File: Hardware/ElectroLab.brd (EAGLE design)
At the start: 175 x 100 mm, 244 parts, among them IC1 LM2902DT, IC10 CD4511BNSR, IC11 PAM8403, IC12 LM2902DT, IC13 ADXL337, IC14 MIC5205, IC2 LM2902DT, IC3 SN74LV08ADR, IC4 SN74LV32ADR, IC5 SN74LV04ADR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

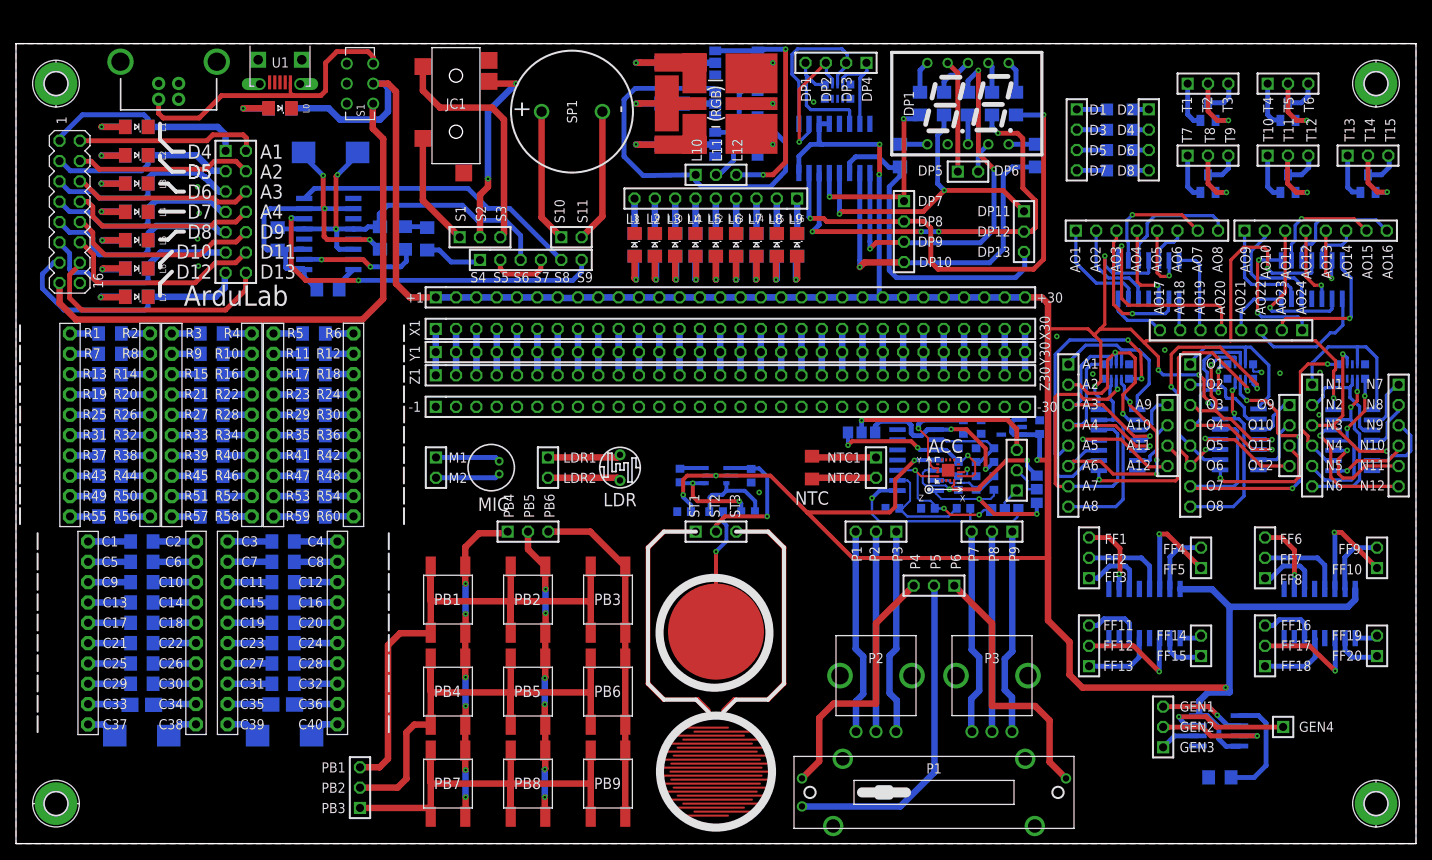
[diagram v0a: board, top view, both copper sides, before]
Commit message: Removed Amplifier after Acc ADXL337
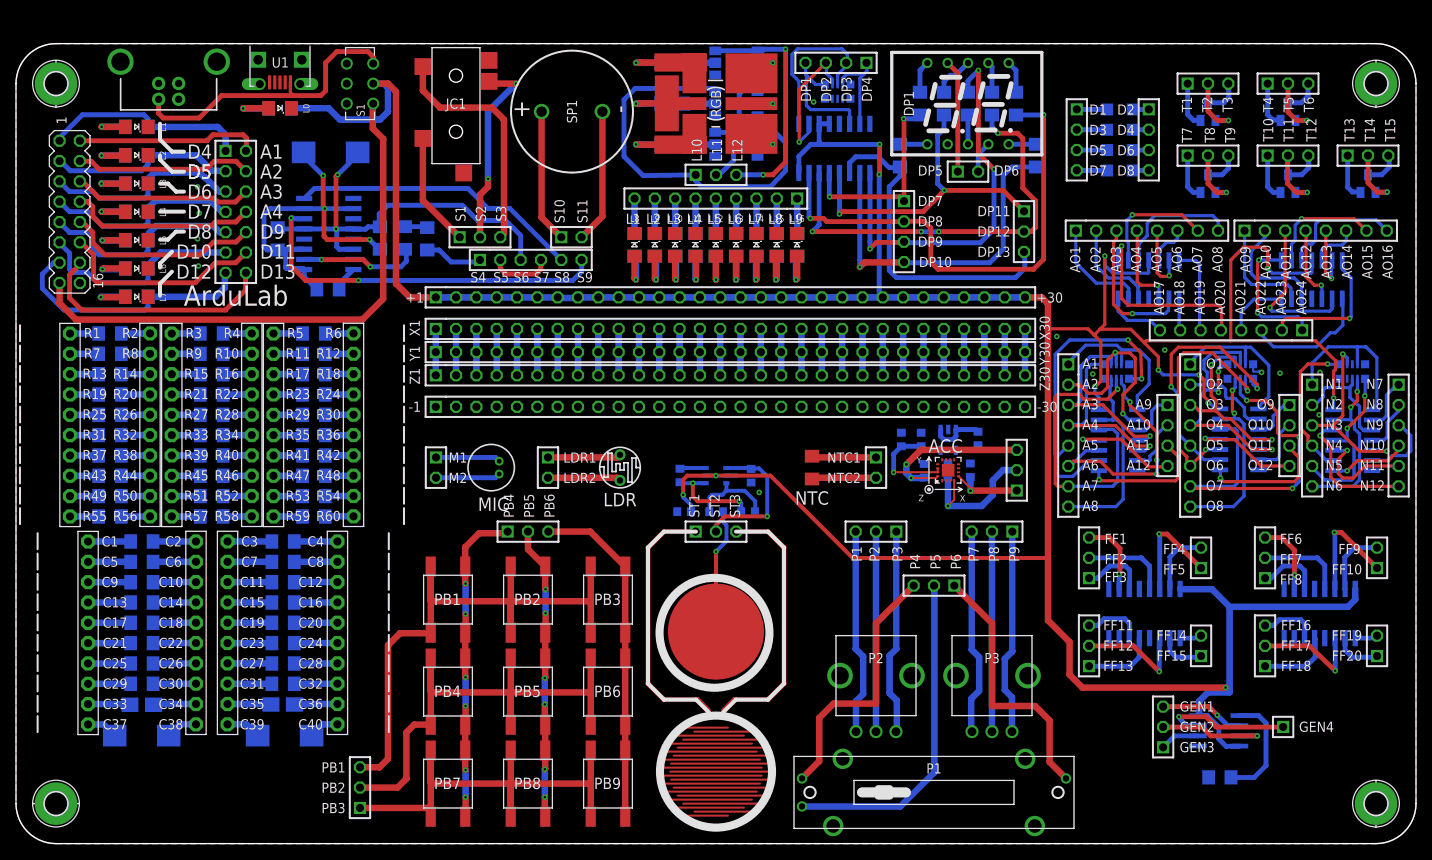
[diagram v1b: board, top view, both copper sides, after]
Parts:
- removed IC12: LM2902DT, Texas Instruments_By_element14_Batch_1:SOIC127P600X175-14N
- removed JMP7, JMP8, JMP9: 0R-JUMPA, jump-0r-smd:A0R-JMP
- removed R61, R62, R63: 1k, SpaceDIY_passive_components:0603
- removed R64, R65, R66: 2k, SpaceDIY_passive_components:0603
- moved IC14 8.09 mm to (116.5, 50.5), turned to 180 degrees
- moved C33 7.91 mm to (110.7, 50.5), turned to 90 degrees
- moved C34 7.84 mm to (120.2, 50.6), turned to 270 degrees
- moved C32 7.66 mm to (113.2, 50.5), turned to 90 degrees
- moved C31 4.73 mm to (113.5, 46.6), turned to 90 degrees
- moved C29 2.42 mm to (119.3, 46.7)
- moved C30 2.06 mm to (116.5, 46.7)
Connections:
- removed net N$124: JMP8.2, PH30.2
- removed net N$127: JMP7.2, PH30.3
- removed net N$128: JMP9.2, PH30.1
- removed net X: IC12.1, JMP7.3, R61.1
- removed net X-: IC12.2, R61.2, R64.1
- removed net Y: IC12.7, JMP8.3, R62.1
- removed net Y-: IC12.6, R62.2, R65.1
- removed net Z: IC12.8, JMP9.3, R63.1
- removed net Z-: IC12.9, R63.2, R66.1
- net GND: no longer IC12.11, R64.2, R65.2, R66.2
- net VCC: no longer IC12.4
- net X+: now also PH30.1; no longer IC12.3, JMP7.1
- net Y+: now also PH30.2; no longer IC12.5, JMP8.1
- net Z+: now also PH30.3; no longer IC12.10, JMP9.1
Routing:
- net Z: track 26.9 -> 0.00 mm, vias 1 -> 0
- net VCC: track 482.8 -> 457.7 mm, vias 14 -> 12
- net N$127: track 24.0 -> 0.00 mm, vias 1 -> 0
- net X: track 21.5 -> 0.00 mm, vias 2 -> 0
- net Y: track 18.2 -> 0.00 mm, vias 2 -> 0
- net Z-: track 13.7 -> 0.00 mm
- net X+: track 23.1 -> 9.94 mm, vias 3 -> 1
- net X-: track 10.6 -> 0.00 mm
- net Y-: track 8.46 -> 0.00 mm
- net Y+: track 23.4 -> 18.6 mm, vias 2 -> 1
- net N$124: track 4.11 -> 0.00 mm
- net 3.3V: track 18.2 -> 14.8 mm
- net GND: track 67.5 -> 64.3 mm, vias 17 -> 16
- net N$128: track 3.05 -> 0.00 mm
- net Z+: track 19.5 -> 21.5 mm, vias 3 -> 2
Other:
- outline, holes or cut-outs redrawn

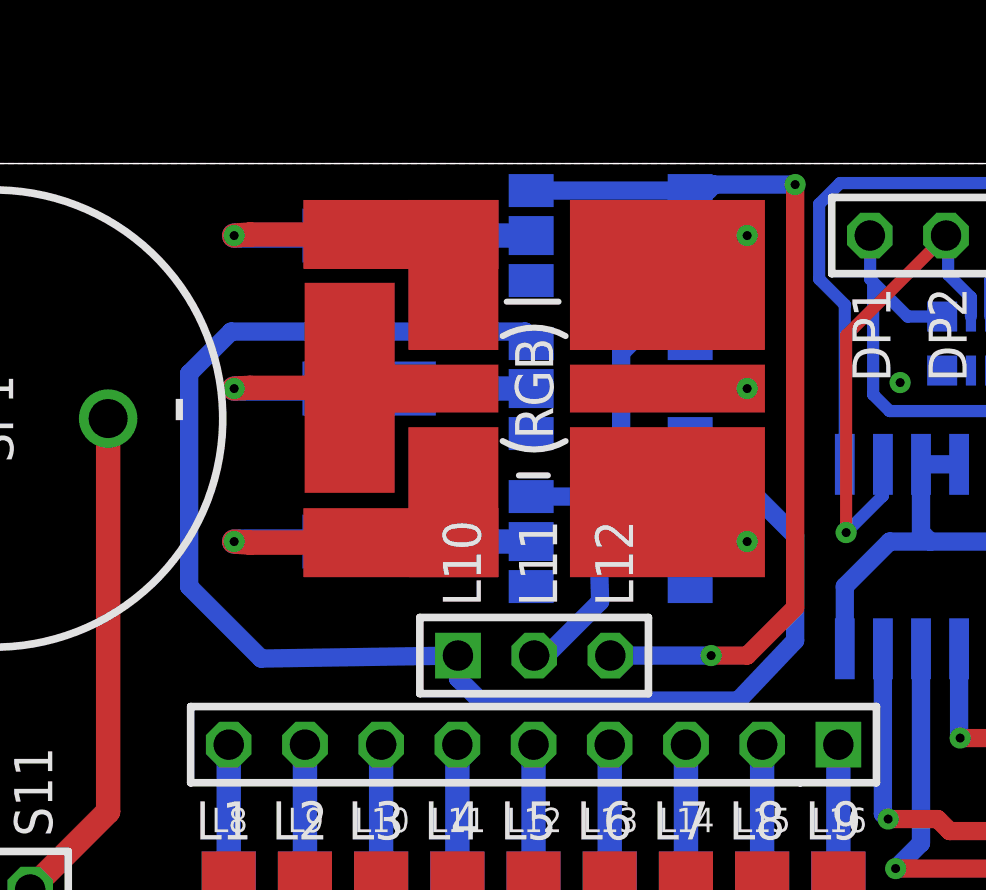
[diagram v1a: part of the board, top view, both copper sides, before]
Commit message: Updated RGB layout
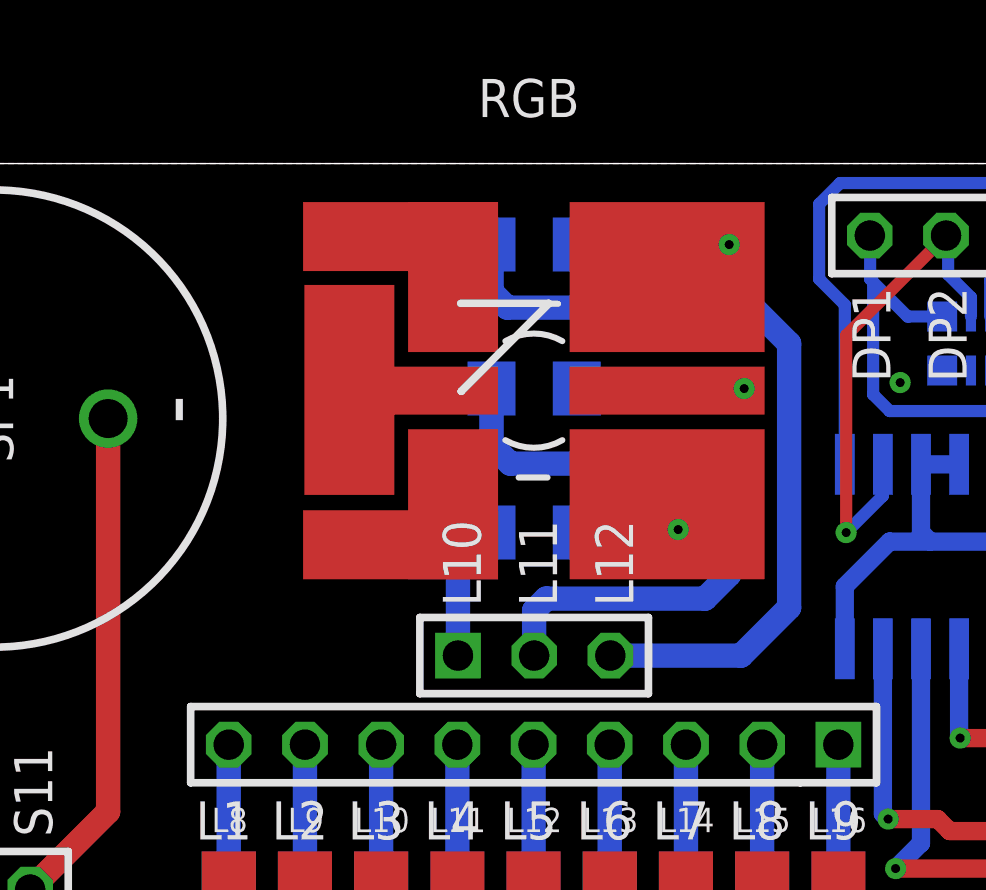
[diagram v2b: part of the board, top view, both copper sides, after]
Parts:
- removed JMP1, JMP2, JMP3, JMP4, JMP5, JMP6: (no value), jump-0r-smd:A0R-JMP
- RGB: device led:OVSTRGBBCR8 -> Passive_components:PLCC6
- moved R57 11.3 mm to (87.5, 87.7), turned to 0 degrees
- moved R59 11.3 mm to (87.5, 97.3), turned to 0 degrees
- moved R58 5.50 mm to (87.5, 92.5), turned to 0 degrees
- moved RGB 0.07 mm to (87.5, 92.4)
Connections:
- removed net N$118: JMP2.2, R58.2
- removed net N$119: JMP3.2, R59.2
- removed net N$120: JMP4.2, RGB.2
- removed net N$121: JMP5.2, RGB.4
- removed net N$122: JMP6.2, RGB.6
- removed net N$309: R58.1, RGB.3
- net B: now also R59.2; no longer JMP1.1, JMP4.1
- net G: now also R58.2; no longer JMP3.1, JMP5.1
- net GND: now also RGB.B-, RGB.G-, RGB.R-; no longer JMP1.3, JMP2.3, JMP3.3, JMP4.3, JMP5.3, JMP6.3
- net N$117: now also R58.1, RGB.G+; no longer JMP1.2, R57.2
- net N$308: now also RGB.R+; no longer RGB.1
- net N$310: now also RGB.B+; no longer RGB.5
- net R: now also R57.2; no longer JMP2.1, JMP6.1
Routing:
- net R: track 50.0 -> 4.56 mm
- net N$309: track 6.93 -> 0.00 mm, vias 1 -> 0
- net G: track 16.5 -> 21.7 mm
- net N$120: track 5.13 -> 0.00 mm, vias 1 -> 0
- net N$122: track 5.10 -> 0.00 mm, vias 1 -> 0
- net N$121: track 4.56 -> 0.00 mm, vias 1 -> 0
- net N$308: track 8.64 -> 4.42 mm
- net N$119: track 3.98 -> 0.00 mm
- net N$118: track 3.98 -> 0.00 mm
- net B: track 29.8 -> 27.6 mm, vias 2 -> 0
- net N$117: track 3.98 -> 5.58 mm, vias 0 -> 1
- net N$310: track 8.64 -> 7.59 mm

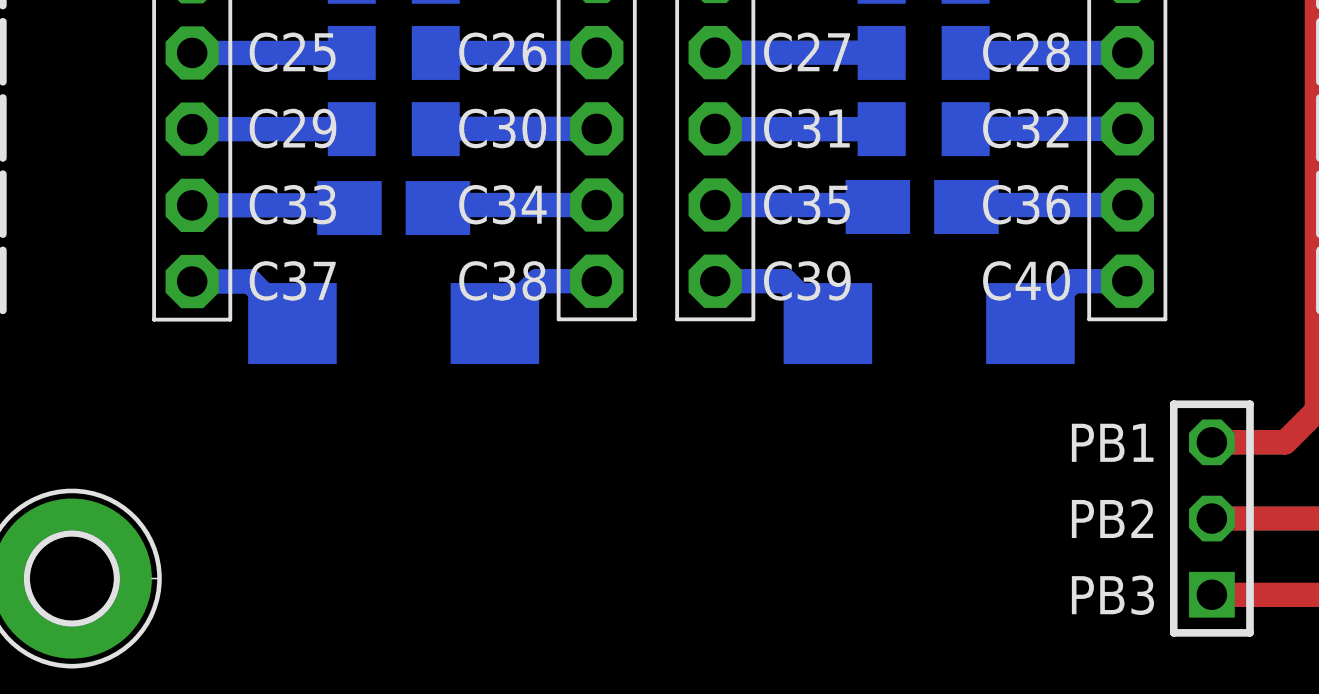
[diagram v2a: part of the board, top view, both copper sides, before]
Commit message: Capacitor area update: - Replaced C19 & C20 for 470uF 7343 (2917) Tantalum capacitors - Added C35 & C36 470uF 7343 (2917) in paralel to C19 & C20 for making 940uF combined - Reviewed Name and Values silkscreen for capacitors
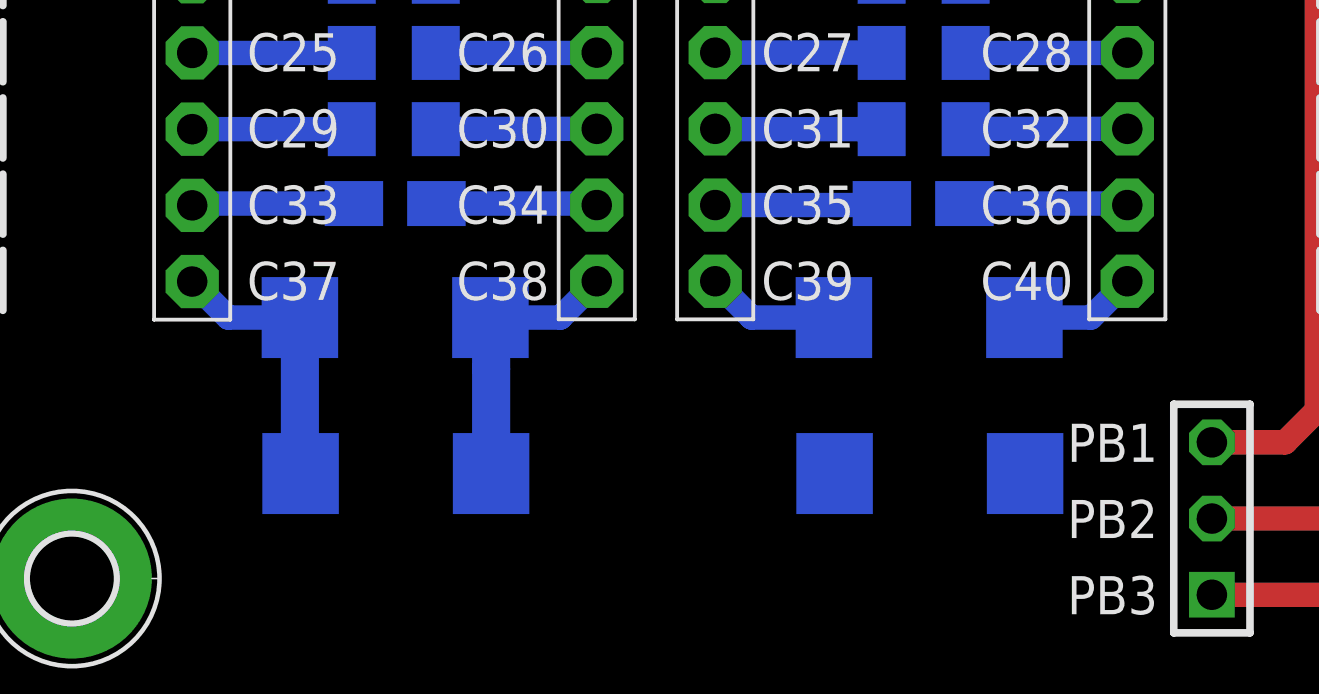
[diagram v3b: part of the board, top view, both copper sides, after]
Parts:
- added C35, C36: 470uF, rcl:D/7343-31R
- C1, C2: value 10p -> 10pF
- C10, C9: value 47n -> 47nF
- C11, C12: value 100n -> 100nF
- C13, C14: value 1u -> 1uF
- C15, C16: value 10u -> 10uF
- C17, C18: value 100u -> 100uF; device rcl:A/3216-18W -> rcl:A/3216-18R
- C19, C20: value 1000u -> 470uF; device rcl:D/7343-31W -> rcl:D/7343-31R
- C3, C4: value 100p -> 100pF
- C5, C6: value 1n -> 1nF
- C7, C8: value 10n -> 10nF
- moved C20 0.21 mm to (15.8, 13.7)
- moved C19 0.20 mm to (33.6, 13.7)
- moved C18 0.16 mm to (15.8, 17.5)
- moved C17 0.12 mm to (33.4, 17.5)
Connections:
- net N$70: now also C35.+
- net N$80: now also C35.-
- net N$90: now also C36.+
- net N$91: now also C36.-
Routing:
- net N$90: track 3.92 -> 9.30 mm
- net N$91: track 3.98 -> 9.26 mm
